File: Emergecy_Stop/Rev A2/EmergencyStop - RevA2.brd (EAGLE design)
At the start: 55 x 25 mm, 12 parts, among them J1 MSTBA2, J2 MSTBA3, J3 NC3FBV2-SW, J4 NC3MAV, T1 EXMACHINA-LOGO-NAME

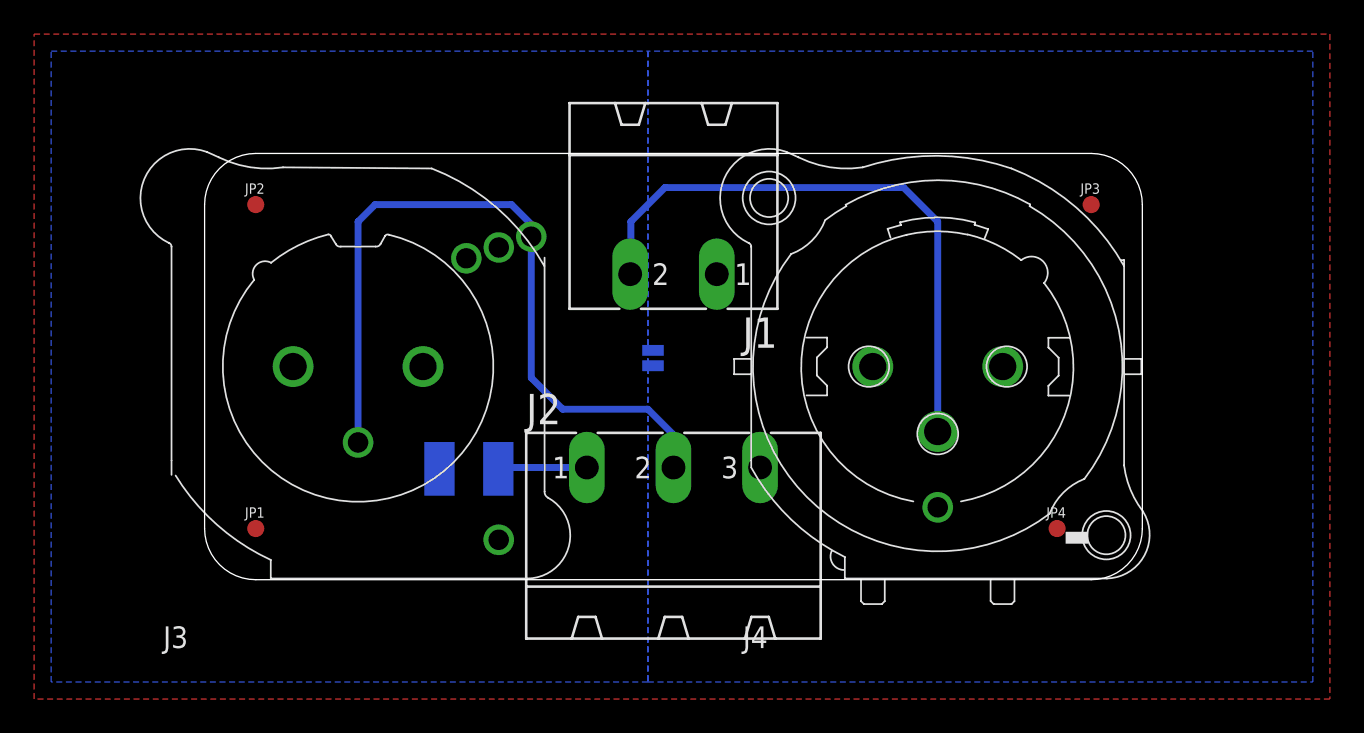
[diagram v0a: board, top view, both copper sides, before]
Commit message: Replace MSTBA with Molex headers and reroute
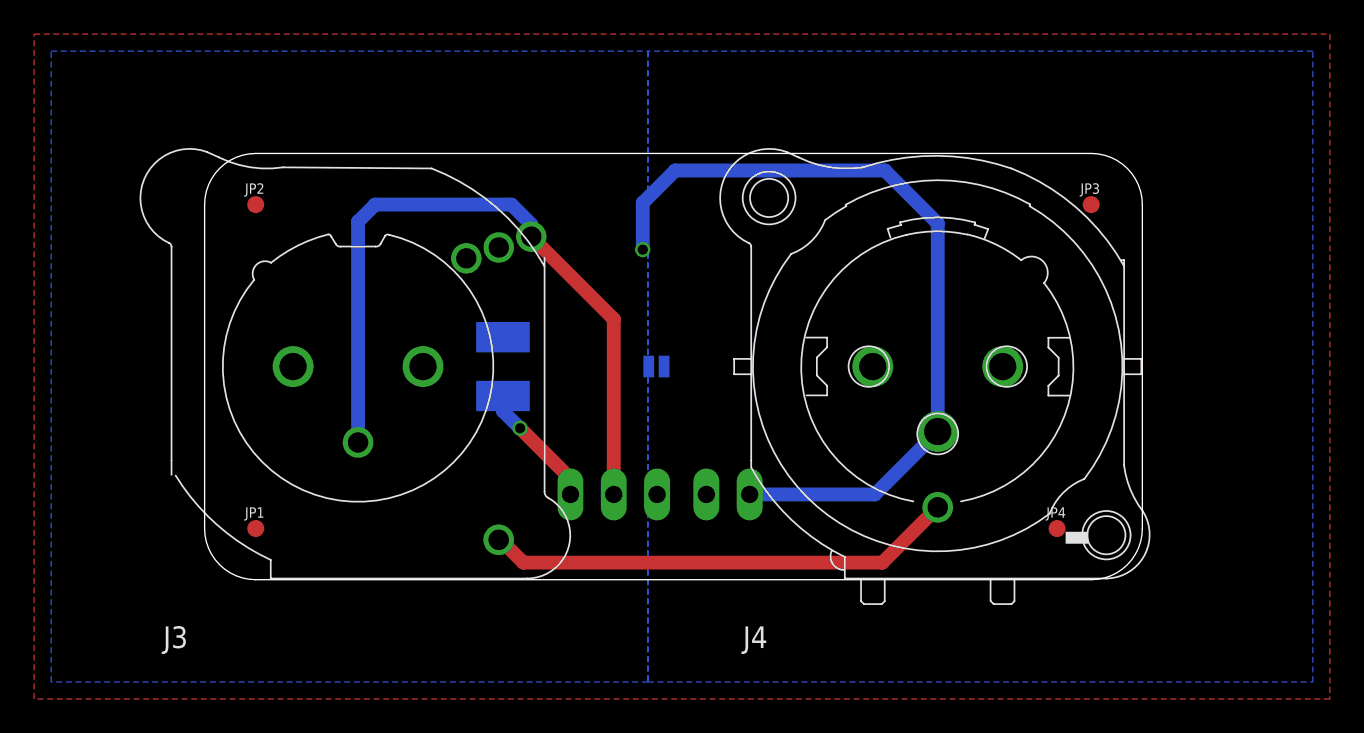
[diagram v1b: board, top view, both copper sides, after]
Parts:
- removed J1: MSTBA2, con-phoenix-508:MSTBA2
- removed J2: MSTBA3, con-phoenix-508:MSTBA3
- added J5: 22-05-7038-03, con-molex:7395-03
- added J6: 22-05-7028-02, con-molex:7395-02
- moved F1 6.32 mm to (17.5, 12.5), turned to 90 degrees
- moved SJ2 0.54 mm to (26.5, 12.5), turned to 180 degrees
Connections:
- removed net N$1: F1.1, J2.1
- new net +24V_IN2: F1.1, J5.1
- new net GND_MECA: J3.G, J4.G
- net +24V_OUT: now also J6.1; no longer J1.1
- net GND: now also J5.3; no longer J2.3
- net SIG_IN: now also J5.2; no longer J2.2
- net SIG_OUT: now also J6.2; no longer J1.2
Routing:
- net GND_MECA: track 0.00 -> 27.6 mm
- net SIG_OUT: track 35.1 -> 46.9 mm, vias 0 -> 1
- net +24V_IN2: track 0.00 -> 7.42 mm, vias 0 -> 1
- net N$1: track 5.23 -> 0.00 mm
- net SIG_IN: track 44.6 -> 41.8 mm
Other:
- board text added: "24V IN"
- board text added: "24V OUT"
- board text added: "GND"
- board text added: "SIG IN"
- board text added: "SIG OUT"
